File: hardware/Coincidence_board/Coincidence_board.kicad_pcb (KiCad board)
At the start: 2 copper layers, 136.8 x 92.5 mm, 69 parts, among them J1 Inputs, J3 POWER_IN, J4 Morpho_Gauche, J7 Morpho_Droite, SW1 SW_1, U1 74HCT74, U2 74HCT74, U3 LM7805_TO220, U4 74HC74, U5 74HC74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

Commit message: Update Coincidence Board / Dephi 2024
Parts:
- added ?: , , F.Cu at (220.5, 71.2)
- added ?: , , F.Cu at (216.4, 145.6)
- added G***: LOGO, LEnsE:Logo_Small, F.Cu at (169.9, 70.2)
- moved C4 135.2 mm to (136.8, 85.0), turned to -90 degrees
- moved U7 108.1 mm to (229.0, 107.1)
- moved R15 107.9 mm to (240.8, 99.4)
- moved C18 107.6 mm to (235.9, 105.8)
- moved R16 106.8 mm to (221.7, 105.9)
- moved C9 106.6 mm to (163.6, 82.4)
- moved R17 100.6 mm to (218.4, 125.6), turned to 90 degrees
- moved R30 99.7 mm to (236.7, 145.0)
- moved R29 96.0 mm to (249.8, 145.1), turned to 180 degrees
- moved U4 82.4 mm to (229.0, 136.4)
- moved R2 82.0 mm to (239.5, 130.3)
- moved R14 81.7 mm to (222.3, 128.8)
- moved R18 78.9 mm to (213.2, 115.4), turned to -90 degrees
- moved C8 76.7 mm to (193.0, 72.8), turned to 180 degrees
- moved C17 68.2 mm to (228.9, 127.8)
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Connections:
- J4 pad 15: unconnected-(J4-Pin_15-Pad15) -> B2out_nuc
- J4 pad 3: unconnected-(J4-Pin_3-Pad3) -> BC2out_nuc
- J4 pad 37: unconnected-(J4-Pin_37-Pad37) -> AC2out_nuc
- J4 pad 40: unconnected-(J4-Pin_40-Pad40) -> C2out_nuc
- J7 pad 13: ABCout_nuc -> unconnected-(J7-Pin_13-Pad13)
- J7 pad 26: AC2out_nuc -> unconnected-(J7-Pin_26-Pad26)
- J7 pad 29: unconnected-(J7-Pin_29-Pad29) -> A2out_nuc
- J7 pad 31: BC2out_nuc -> unconnected-(J7-Pin_31-Pad31)
- J7 pad 32: AB2out_nuc -> unconnected-(J7-Pin_32-Pad32)
- J7 pad 33: unconnected-(J7-Pin_33-Pad33) -> ABCout_nuc
- J7 pad 5: A2out_nuc -> AB2out_nuc
- J7 pad 7: B2out_nuc -> unconnected-(J7-Pin_7-Pad7)
- U1 pad 2: unconnected-(U1A-D-Pad2) -> GND
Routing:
- net 5V: track 0.00 -> 352.0 mm, vias 0 -> 5
- net 3.3V_NUC: track 0.00 -> 130.3 mm
- net A2in: track 0.00 -> 123.7 mm, vias 0 -> 2
- net VIN: track 0.00 -> 101.6 mm
- net GND: track 0.00 -> 95.4 mm, vias 0 -> 7
- net Net-(U4A-C): track 0.00 -> 91.9 mm
- net Net-(U4B-Q): track 0.00 -> 87.7 mm, vias 0 -> 2
- net C2in: track 0.00 -> 75.4 mm
- net Net-(U4B-~{Q}): track 0.00 -> 75.1 mm, vias 0 -> 4
- net AB2out_nuc: track 0.00 -> 61.3 mm
- net B2in: track 0.00 -> 54.2 mm, vias 0 -> 1
- net Ain: track 0.00 -> 52.5 mm
- net A2out_nuc: track 0.00 -> 46.2 mm
- net Net-(U1A-~{Q}): track 0.00 -> 38.4 mm
- net BC2out_nuc: track 0.00 -> 35.2 mm
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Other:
- board size 136.8 x 92.5 mm -> 136.8 x 85 mm
- board text added: "7-12V"
- board text added: "GND"
- board text added: "Quantum Interference LEnsE / 2024 / Dephi Project"

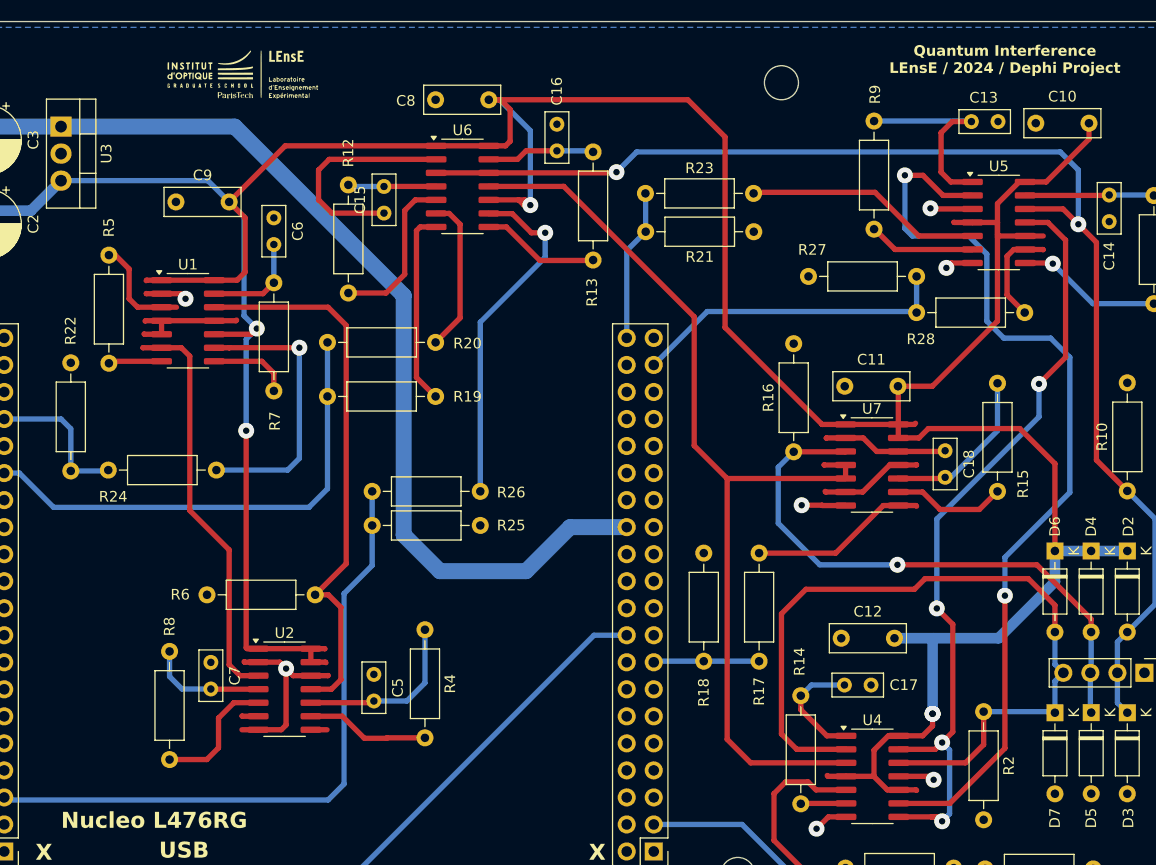
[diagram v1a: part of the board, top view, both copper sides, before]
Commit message: Update Schematics of Electronic Board
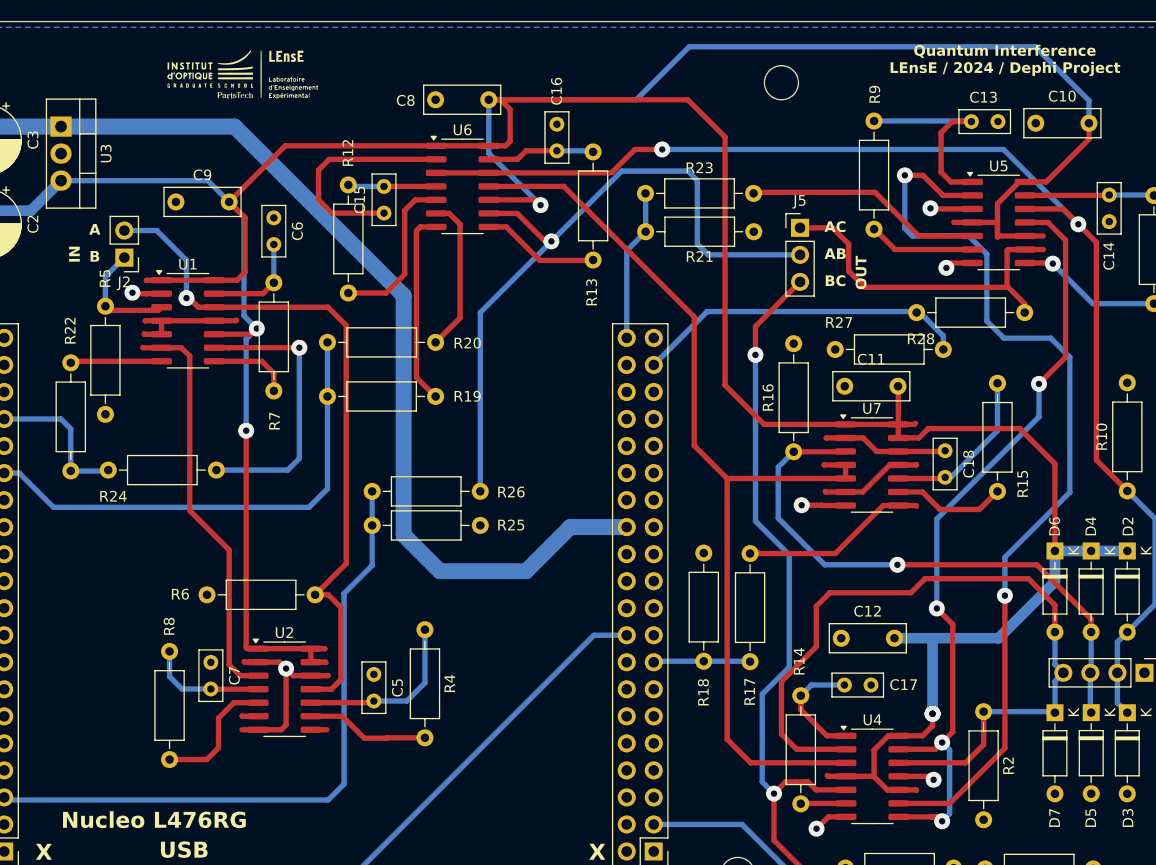
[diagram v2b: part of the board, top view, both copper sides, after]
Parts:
- added J2: chan2_in, Connector_PinHeader_2.54mm:PinHeader_1x02_P2.54mm_Vertical, F.Cu at (158.8, 87.6)
- added J5: chan3_out, Connector_PinHeader_2.54mm:PinHeader_1x03_P2.54mm_Vertical, F.Cu at (222.2, 84.8)
- moved R27 7.31 mm to (225.6, 96.3)
- moved R5 4.81 mm to (157.0, 92.2)
- moved R17 0.85 mm to (217.6, 125.6)
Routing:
- net BC2out: track 19.7 -> 72.4 mm, vias 0 -> 2
- net 5V: track 352.0 -> 397.6 mm
- net AB2out: track 32.9 -> 66.1 mm
- net AC2out: track 9.66 -> 33.3 mm
- net Ain: track 52.5 -> 66.1 mm, vias 0 -> 1
- net A2in: track 123.7 -> 120.4 mm
- net GND: track 95.4 -> 97.9 mm
- net C2in: track 75.4 -> 73.8 mm
- net AC2out_nuc: track 30.2 -> 31.5 mm
- net B2out: track 16.7 -> 17.6 mm
- net Bin: track 10.0 -> 10.9 mm
- net B2out_nuc: track 9.94 -> 9.11 mm
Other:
- board text added: "A"
- board text added: "AB"
- board text added: "AC"
- board text added: "B"
- board text added: "BC"
- board text added: "IN"
- board text added: "OUT"

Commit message: Update Schematic
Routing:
- net 5V: track 397.6 -> 400.3 mm
- net Net-(U7B-Q): track 10.7 -> 9.96 mm
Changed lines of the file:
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@@
 		(tags "Through hole pin header THT 1x03 2.54mm single row")
 		(property "Reference" "J5"
-			(at 0 -2.54 360)
+			(at 0 -2.54 0)
 			(layer "F.SilkS")
 			(effects
@@
 		)
 		(property "Value" "chan3_out"
-			(at 0 7.41 360)
+			(at 0 7.41 0)
 			(layer "F.Fab")
 			(effects
@@
 		(tags "Resistor Axial_DIN0207 series Axial Horizontal pin pitch 10.16mm 0.25W = 1/4W length 6.3mm diameter 2.5mm")
 		(property "Reference" "R5"
-			(at -2.6 0 90)
+			(at 10.198 -2.428 90)
 			(layer "F.SilkS")
 			(effects
@@
 		(tags "Resistor Axial_DIN0207 series Axial Horizontal pin pitch 10.16mm 0.25W = 1/4W length 6.3mm diameter 2.5mm")
 		(property "Reference" "R27"
-			(at 0.36 -2.5 360)
+			(at 0.36 -2.5 0)
 			(layer "F.SilkS")
 			(effects
@@
 		)
 		(property "Value" "3.3k"
-			(at 5.08 2.37 360)
+			(at 5.08 2.37 0)
 			(layer "F.Fab")
 			(effects
@@
 		)
 		(fp_text user "${REFERENCE}"
-			(at 5.08 0 360)
+			(at 5.08 0 0)
 			(layer "F.Fab")
 			(effects
@@
 		(tags "SO SO")
 		(property "Reference" "U7"
-			(at 0 -5.28 0)
+			(at 2.595 5.68 0)
 			(layer "F.SilkS")
 			(effects
@@
 		(tags "Resistor Axial_DIN0207 series Axial Horizontal pin pitch 10.16mm 0.25W = 1/4W length 6.3mm diameter 2.5mm")
 		(property "Reference" "R28"
-			(at 0.4 2.5 0)
+			(at 9.7 2.5 0)
 			(layer "F.SilkS")
 			(effects
@@
 		)
 		(fp_text user "${REFERENCE}"
-			(at 0 1.27 270)
+			(at 0 1.27 -90)
 			(layer "F.Fab")
 			(effects
@@
 		(tags "C Rect series Radial pin pitch 5.00mm  length 7mm width 2.5mm Capacitor")
 		(property "Reference" "C11"
-			(at 2.5 -2.5 0)
+			(at 7.95 0.08 0)
 			(layer "F.SilkS")
 			(effects
@@
 		(tags "C Rect series Radial pin pitch 2.50mm  length 4.6mm width 2mm Capacitor")
 		(property "Reference" "C15"
-			(at 1.25 -2.25 -90)
+			(at -3.15 0.05 -90)
 			(layer "F.SilkS")
 			(effects
@@
 	)
 	(segment
-		(start 242.9 103.7)
-		(end 246.2 107)
+		(start 170.47 77.13)
+		(end 168.6 79)
 		(width 0.5)
 		(layer "F.Cu")
@@
 	)
 	(segment
-		(start 173.87 77.13)
-		(end 168.6 82.4)
-		(width 0.5)
-		(layer "F.Cu")
-		(net 59)
-	)
-	(segment
 		(start 240.8 82.562316)
 		(end 240.8 85.5)
@@
 	)
 	(segment
-		(start 229.18 136.38)
-		(end 229.2 136.36)
+		(start 229.2 136.36)
+		(end 229.2 133.4)
 		(width 0.5)
 		(layer "F.Cu")
@@
 	)
 	(segment
-		(start 188.05 77.13)
-		(end 173.87 77.13)
-		(width 0.5)
-		(layer "F.Cu")
-		(net 59)
-	)
-	(segment
 		(start 240.8 85.5)
 		(end 240.9 85.6)
@@
 	)
 	(segment
+		(start 246.2 107)
+		(end 246.2 115.2)
+		(width 0.5)
+		(layer "F.Cu")
+		(net 59)
+	)
+	(segment
 		(start 245.38 80.52)
 		(end 243.4 80.52)
@@
 	)
 	(segment
-		(start 231.52 137.65)
-		(end 230.45 137.65)
-		(width 0.5)
-		(layer "F.Cu")
-		(net 59)
-	)
-	(segment
-		(start 233.42 104.58)
-		(end 234.3 103.7)
+		(start 238.45 84.33)
+		(end 236.73 84.33)
 		(width 0.5)
 		(layer "F.Cu")
@@
 	)
 	(segment
-		(start 238.45 84.33)
-		(end 236.73 84.33)
+		(start 188.05 77.13)
+		(end 170.47 77.13)
 		(width 0.5)
 		(layer "F.Cu")
@@
 	)
 	(segment
-		(start 229.2 133.915001)
-		(end 230.545001 132.57)
+		(start 229.18 136.38)
+		(end 229.2 136.36)
 		(width 0.5)
 		(layer "F.Cu")
@@
 	)
 	(segment
-		(start 230.45 137.65)
-		(end 229.18 136.38)
+		(start 230.03 132.57)
+		(end 231.52 132.57)
 		(width 0.5)
 		(layer "F.Cu")
@@
 	)
 	(segment
+		(start 229.75 137.65)
+		(end 229.18 137.08)
+		(width 0.5)
+		(layer "F.Cu")
+		(net 59)
+	)
+	(segment
 		(start 162.25 89.755)
 		(end 167.2 89.755)
@@
 	)
 	(segment
+		(start 231.48 104.58)
+		(end 233.92 104.58)
+		(width 0.5)
+		(layer "F.Cu")
+		(net 59)
+	)
+	(segment
 		(start 215.2 76.3)
 		(end 211.7 72.8)
@@
 	)
 	(segment
-		(start 229.2 136.36)
-		(end 229.2 133.915001)
+		(start 229.2 133.4)
+		(end 230.03 132.57)
 		(width 0.5)
 		(layer "F.Cu")
@@
 	)
 	(segment
-		(start 246.2 107)
-		(end 246.2 115.2)
+		(start 168.6 79)
+		(end 168.6 82.4)
 		(width 0.5)
 		(layer "F.Cu")
@@
 	)
 	(segment
-		(start 176.28 125.65)
-		(end 177.65 125.65)
+		(start 231.52 137.65)
+		(end 229.75 137.65)
 		(width 0.5)
 		(layer "F.Cu")
@@
 	)
 	(segment
-		(start 230.545001 132.57)
-		(end 231.52 132.57)
+		(start 176.28 125.65)
+		(end 177.65 125.65)
 		(width 0.5)
 		(layer "F.Cu")
@@
 	)
 	(segment
-		(start 234.3 103.7)
-		(end 242.9 103.7)
+		(start 224.88 136.38)
+		(end 224.8 136.3)
 		(width 0.5)
 		(layer "F.Cu")
@@
 	)
 	(segment
-		(start 224.88 136.38)
-		(end 224.8 136.3)
+		(start 233.92 104.58)
+		(end 234.8 103.7)
+		(width 0.5)
+		(layer "F.Cu")
+		(net 59)
+	)
+	(segment
+		(start 242.9 103.7)
+		(end 246.2 107)
 		(width 0.5)
 		(layer "F.Cu")
@@
 	)
 	(segment
-		(start 231.48 104.58)
-		(end 233.42 104.58)
+		(start 234.8 103.7)
+		(end 242.9 103.7)
 		(width 0.5)
 		(layer "F.Cu")
@@
 	)
 	(segment
+		(start 229.18 137.08)
+		(end 229.18 136.38)
+		(width 0.5)
+		(layer "F.Cu")
+		(net 59)
+	)
+	(segment
 		(start 194.57 77.13)
 		(end 195 76.7)
@@
 	)
 	(segment
-		(start 233.76 109.66)
-		(end 235.4 111.3)
+		(start 234.56 109.66)
+		(end 235.3 110.4)
 		(width 0.5)
 		(layer "F.Cu")
@@
 	)
 	(segment
-		(start 235.4 111.3)
-		(end 239.1 111.3)
+		(start 240 110.4)
+		(end 240.8 109.6)
 		(width 0.5)
 		(layer "F.Cu")
@@
 	)
 	(segment
-		(start 231.48 109.66)
-		(end 233.76 109.66)
+		(start 235.3 110.4)
+		(end 240 110.4)
 		(width 0.5)
 		(layer "F.Cu")
@@
 	)
 	(segment
-		(start 239.1 111.3)
-		(end 240.8 109.6)
+		(start 231.48 109.66)
+		(end 234.56 109.66)
 		(width 0.5)
 		(layer "F.Cu")

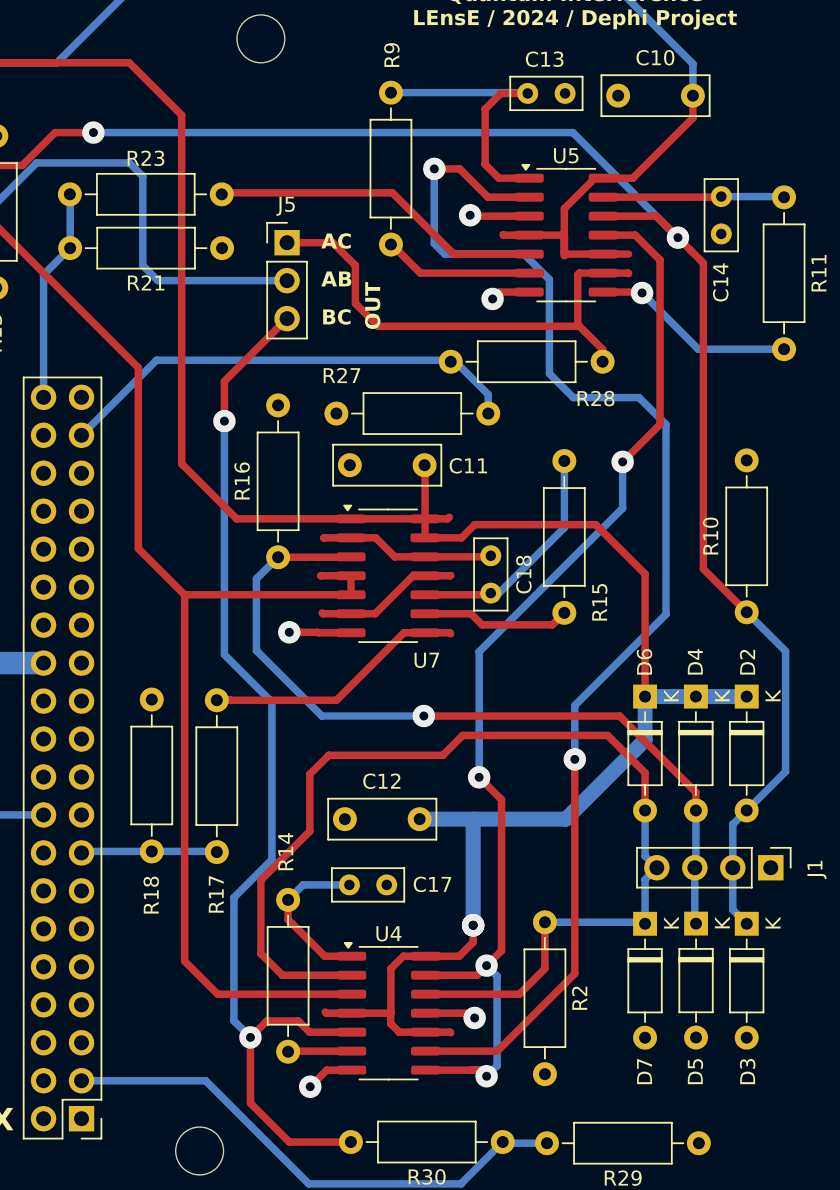
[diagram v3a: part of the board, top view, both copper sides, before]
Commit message: Update Coincidence Board / New schematics (Anouk - Jeanne)
Test with Nucleo L476RG ? Not fast enough ??
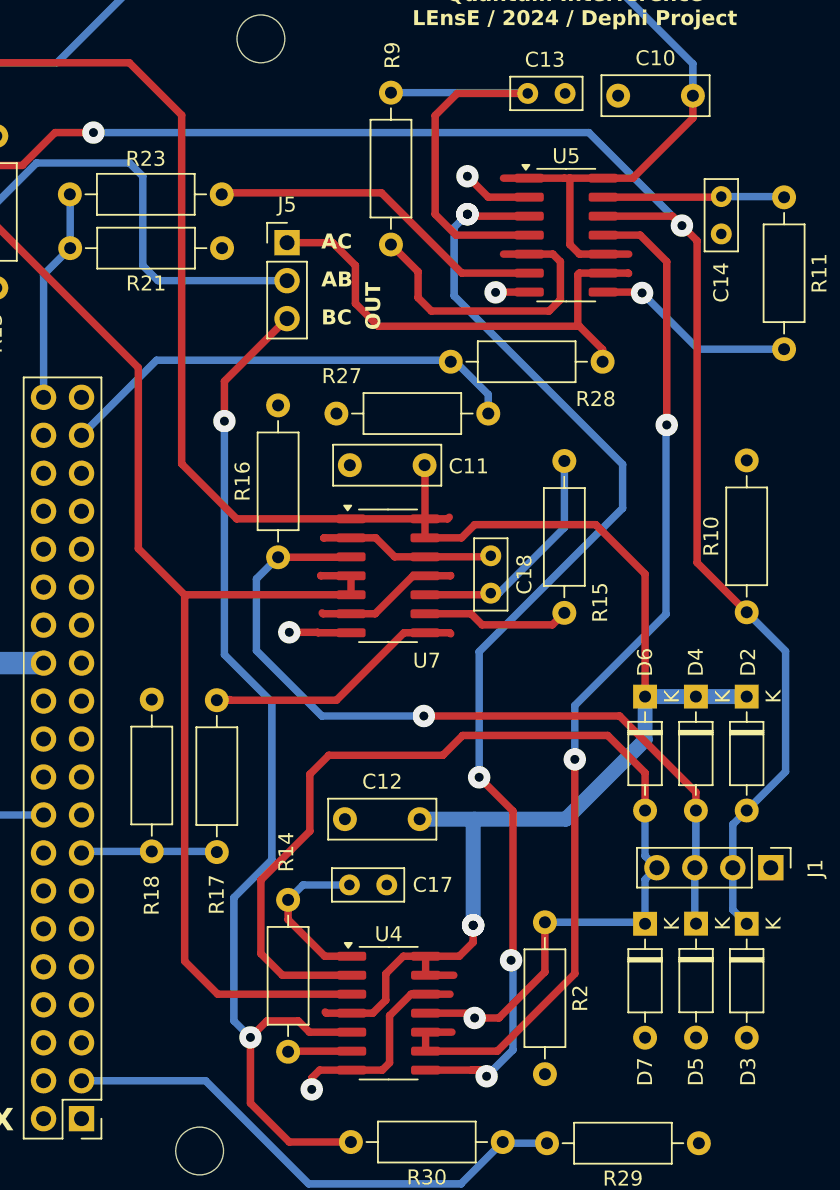
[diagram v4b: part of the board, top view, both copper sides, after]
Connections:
- C13 pad 2: Net-(U5A-~{R}) -> Net-(U5A-~{S})
- R9 pad 1: Net-(U5A-~{R}) -> Net-(U5A-~{S})
- R9 pad 2: Net-(U5A-~{Q}) -> Net-(U5A-Q)
- U4 pad 10: 5V -> Net-(U4B-Q)
- U4 pad 11: GND -> C2in
- U4 pad 12: C2in -> GND
- U4 pad 13: Net-(U4B-~{Q}) -> 5V
- U5 pad 1: Net-(U5A-~{R}) -> 5V
- U5 pad 11: Net-(U4B-~{Q}) -> Net-(U4B-Q)
- U5 pad 2: Net-(U4B-Q) -> GND
- U5 pad 3: GND -> Net-(U4B-~{Q})
- U5 pad 4: 5V -> Net-(U5A-~{S})
- U5 pad 5: C2out -> Net-(U5A-Q)
- U5 pad 6: Net-(U5A-~{Q}) -> C2out
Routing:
- net Net-(U5A-~{S}): track 0.00 -> 29.5 mm
- net Net-(U5A-Q): track 0.00 -> 21.1 mm
- net Net-(U5A-~{R}): track 19.5 -> 0.00 mm
- net Net-(U4B-Q): track 87.7 -> 70.4 mm
- net Net-(U5A-~{Q}): track 10.0 -> 0.00 mm
- net GND: track 97.9 -> 105.8 mm, vias 7 -> 6
- net 5V: track 400.3 -> 396.7 mm
- net Net-(U4B-~{Q}): track 75.1 -> 77.7 mm, vias 4 -> 5
- net C2in: track 73.8 -> 74.8 mm, vias 0 -> 1
- net A2in: track 120.4 -> 121.0 mm
- net C2out: track 22.3 -> 22.8 mm

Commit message: Update Coincidence Board / 2025 version
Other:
- board text added: "Quantum Interference LEnsE / 2025 / Dephi Project"
- board text removed: "Quantum Interference LEnsE / 2024 / Dephi Project"
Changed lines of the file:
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@@
 		)
 	)
-	(gr_text "Quantum Interference\nLEnsE / 2024 / Dephi Project"
+	(gr_text "Quantum Interference\nLEnsE / 2025 / Dephi Project"
 		(at 241.5 70.4 0)
 		(layer "F.SilkS")
